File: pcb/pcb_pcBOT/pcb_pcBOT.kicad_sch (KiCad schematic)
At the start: 0 parts

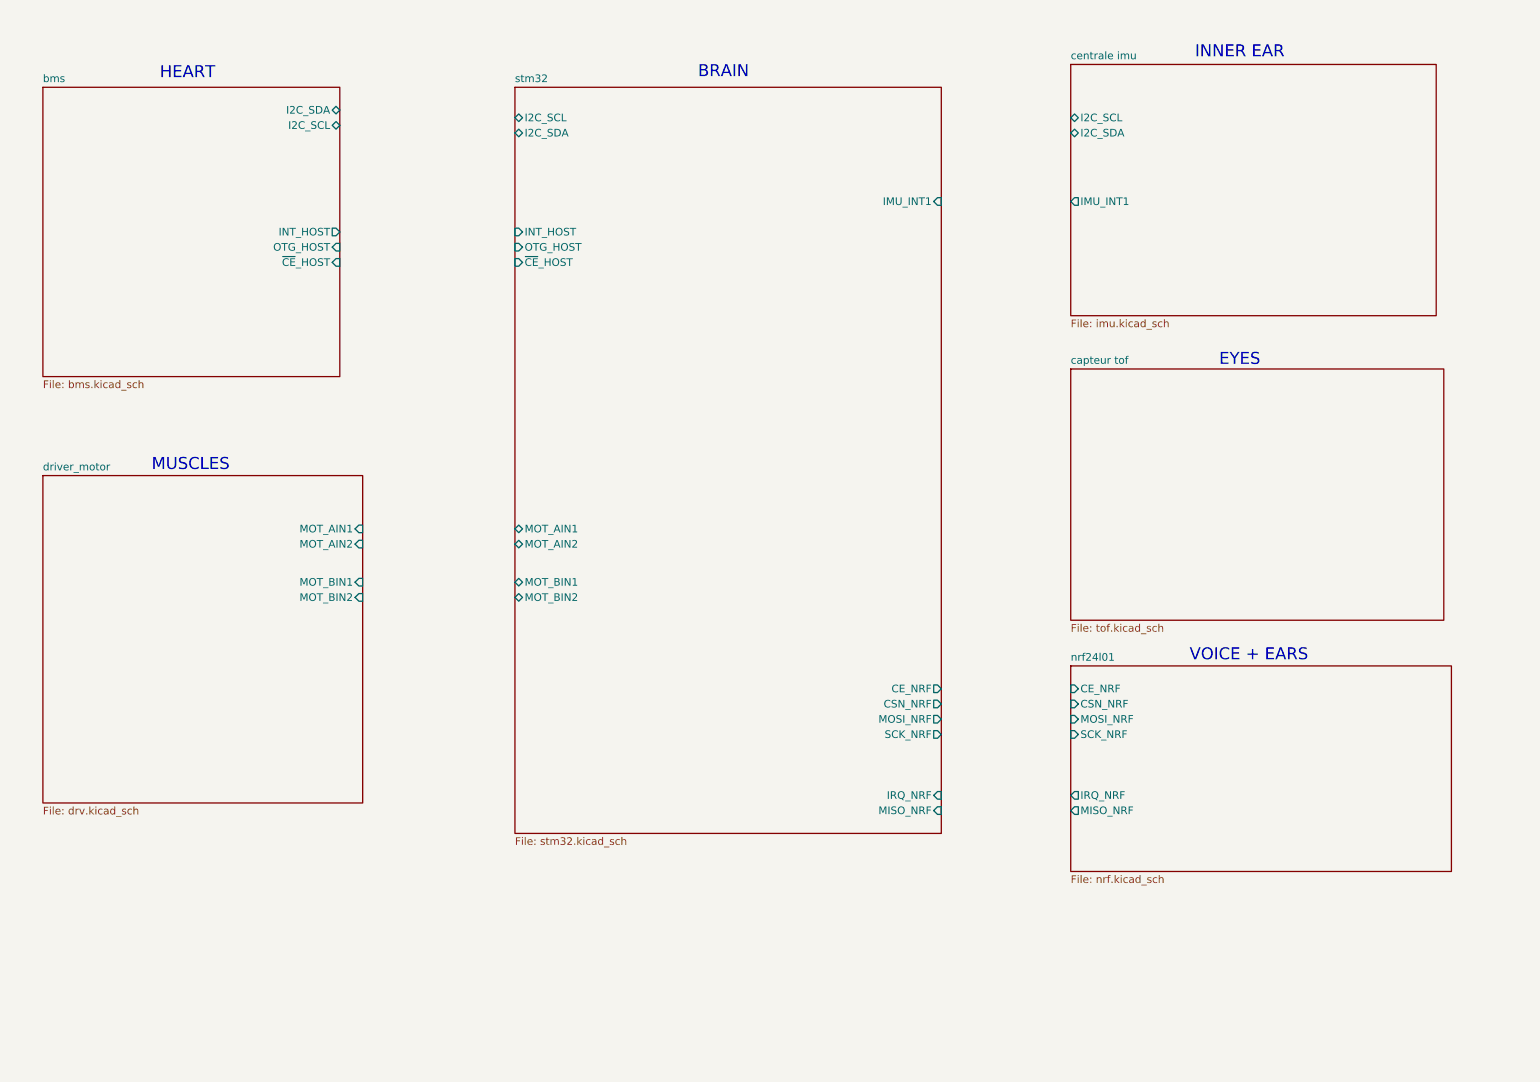
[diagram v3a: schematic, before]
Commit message: complement tof et connections, mise a jour du firmware
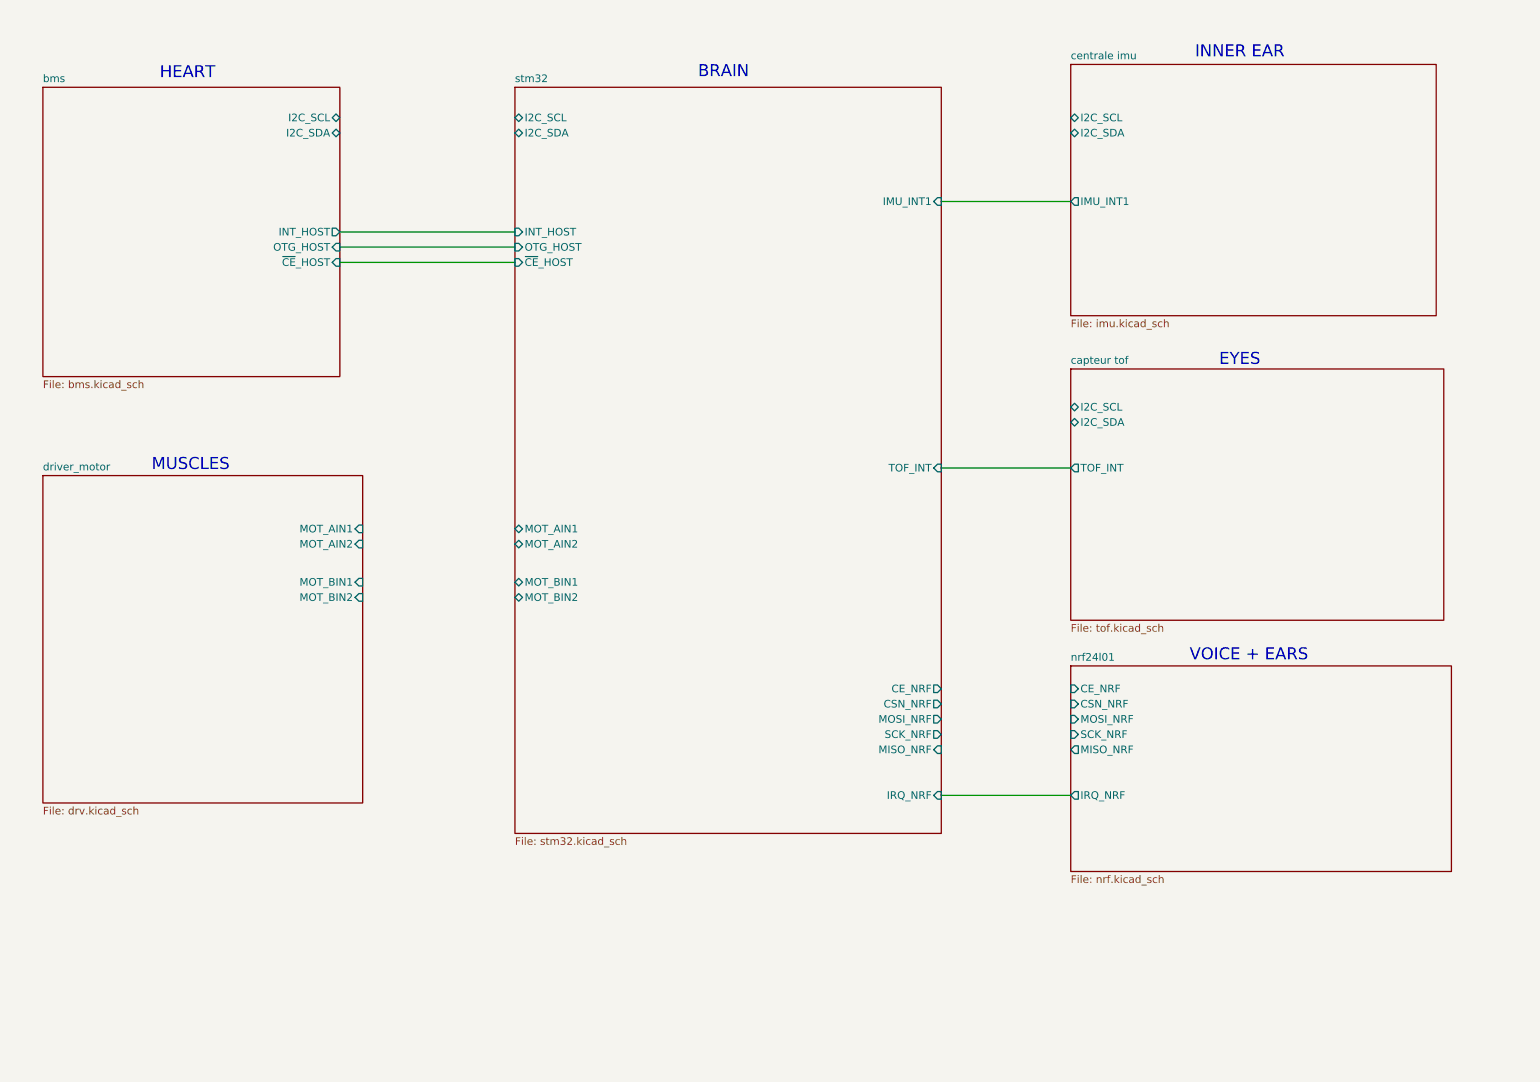
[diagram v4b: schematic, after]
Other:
- sheet capteur tof ports: added I2C_SCL, I2C_SDA, TOF_INT; removed none
- sheet stm32 ports: added TOF_INT; removed none
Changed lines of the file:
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@@
+		)
+	)
+	(wire
+		(pts
+			(xy 177.8 91.44) (xy 199.39 91.44)
+		)
+		(stroke
+			(width 0)
+			(type default)
+		)
+	)
+	(wire
+		(pts
+			(xy 177.8 46.99) (xy 199.39 46.99)
+		)
+		(stroke
+			(width 0)
+			(type default)
+		)
+	)
+	(wire
+		(pts
+			(xy 77.47 57.15) (xy 106.68 57.15)
+		)
+		(stroke
+			(width 0)
+			(type default)
+		)
+	)
+	(wire
+		(pts
+			(xy 177.8 146.05) (xy 199.39 146.05)
+		)
+		(stroke
+			(width 0)
+			(type default)
+		)
+	)
+	(wire
+		(pts
+			(xy 77.47 52.07) (xy 106.68 52.07)
+		)
+		(stroke
+			(width 0)
+			(type default)
+		)
+	)
+	(wire
+		(pts
+			(xy 77.47 54.61) (xy 106.68 54.61)
+		)
+		(stroke
+			(width 0)
+			(type default)
 		)
 	)
@@
 		)
 		(pin "MISO_NRF" output
-			(at 199.39 148.59 180)
+			(at 199.39 138.43 180)
 			(effects
 				(font
@@
 			)
 		)
+		(pin "TOF_INT" output
+			(at 199.39 91.44 180)
+			(effects
+				(font
+					(size 1.27 1.27)
+				)
+				(justify left)
+			)
+		)
+		(pin "I2C_SCL" bidirectional
+			(at 199.39 81.28 180)
+			(effects
+				(font
+					(size 1.27 1.27)
+				)
+				(justify left)
+			)
+		)
+		(pin "I2C_SDA" bidirectional
+			(at 199.39 83.82 180)
+			(effects
+				(font
+					(size 1.27 1.27)
+				)
+				(justify left)
+			)
+		)
 		(instances
 			(project "pcb_pcBOT"
@@
 		)
 		(pin "MISO_NRF" input
-			(at 177.8 148.59 0)
+			(at 177.8 138.43 0)
 			(effects
 				(font
@@
 		(pin "SCK_NRF" output
 			(at 177.8 135.89 0)
+			(effects
+				(font
+					(size 1.27 1.27)
+				)
+				(justify right)
+			)
+		)
+		(pin "TOF_INT" input
+			(at 177.8 91.44 0)
 			(effects
 				(font
@@
 		)
 		(pin "I2C_SDA" bidirectional
-			(at 77.47 31.75 0)
+			(at 77.47 35.56 0)
 			(effects
 				(font
@@
 		)
 		(pin "I2C_SCL" bidirectional
-			(at 77.47 34.29 0)
-			(effects
-				(font
+			(at 77.47 33.02 0)
+			(effects
+				(font

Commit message: corrections d'erreurs et liasons bus i2c et spi
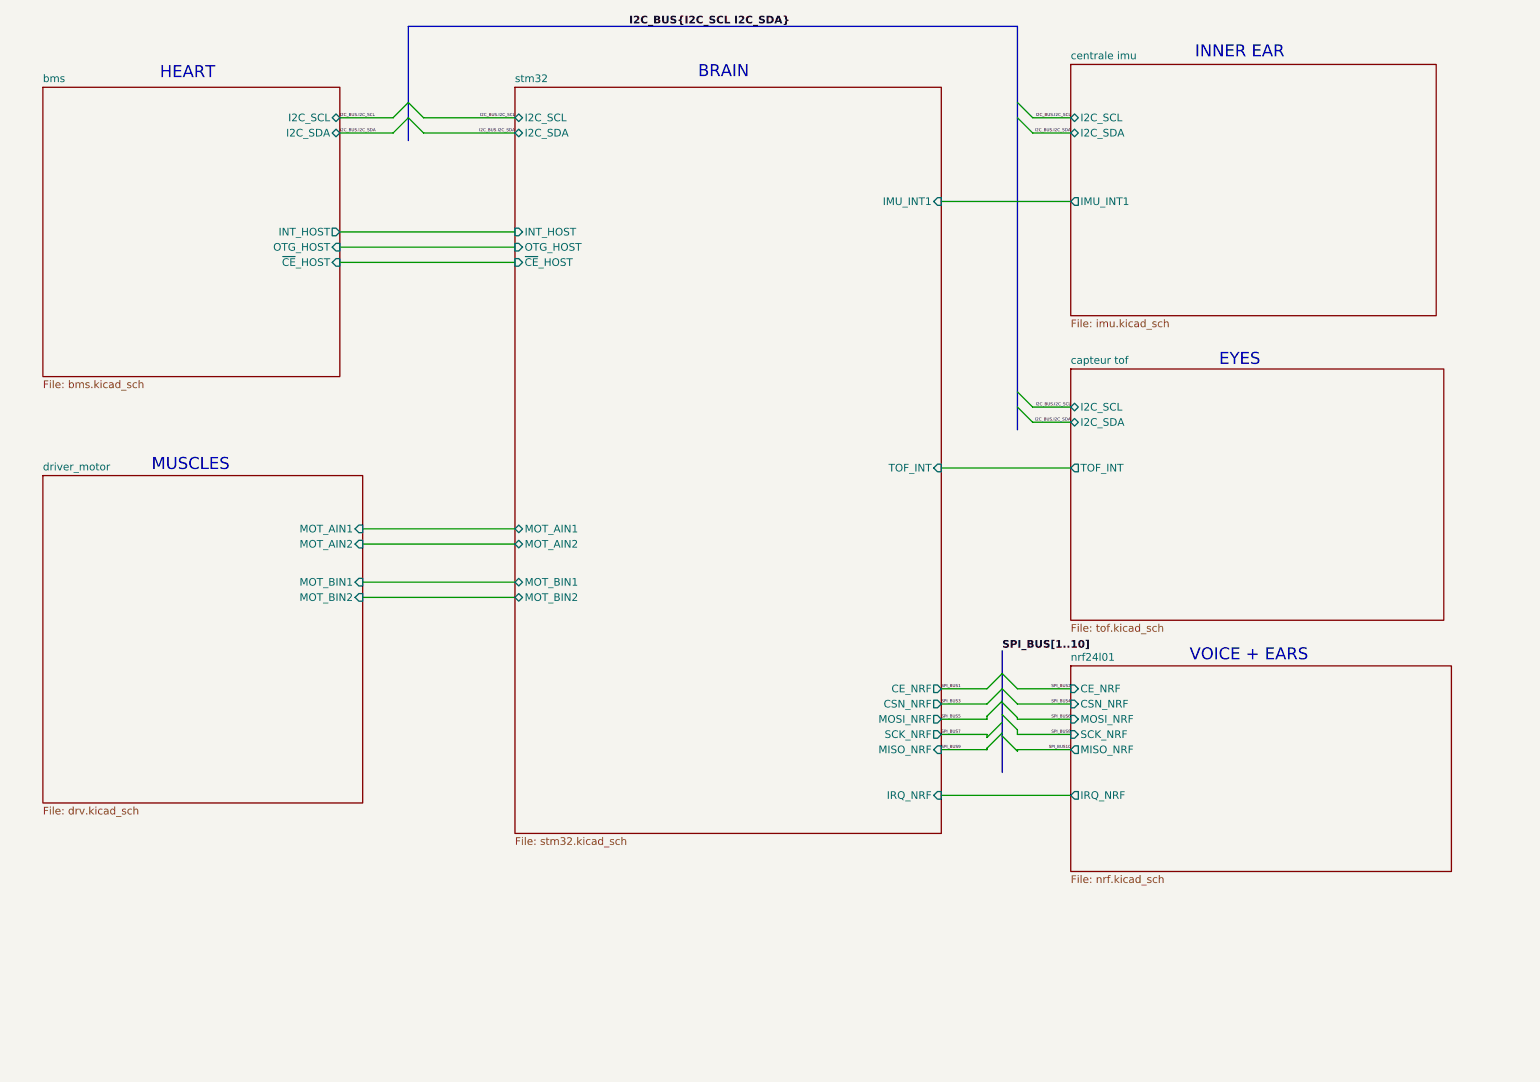
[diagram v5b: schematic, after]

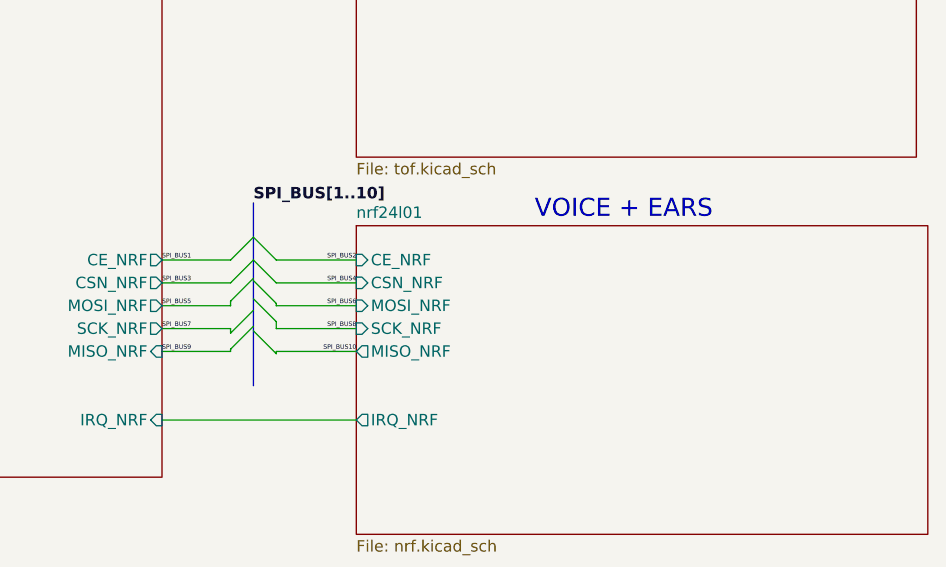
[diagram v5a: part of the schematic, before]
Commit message: Ajout empreintes (incomplet) + test erc correct
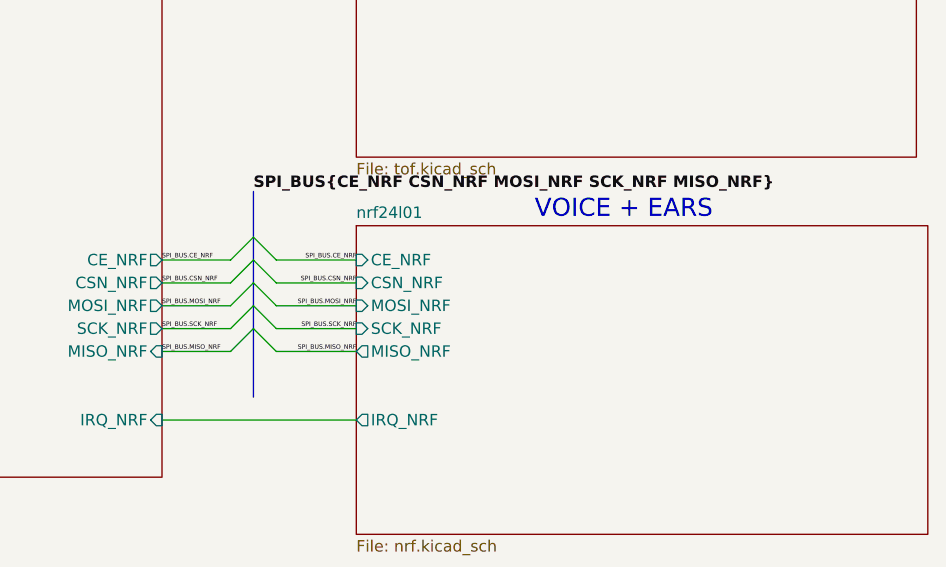
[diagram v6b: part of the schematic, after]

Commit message: fin de schematique
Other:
- sheet bms ports: added INT_BMS; removed INT_HOST
- sheet capteur tof ports: added TOF_INT1, TOF_INT2, TOF_INT3, XSHUT1, XSHUT2, XSHUT3; removed TOF_INT
- sheet stm32 ports: added INT_BMS, TOF_INT1, TOF_INT2, TOF_INT3, XSHUT1, XSHUT2, XSHUT3; removed INT_HOST, TOF_INT
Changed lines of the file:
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@@
-	(wire
-		(pts
-			(xy 177.8 91.44) (xy 199.39 91.44)
-		)
-		(stroke
-			(width 0)
-			(type default)
-		)
-	)
 	(wire
 		(pts
@@
 		)
 	)
+	(wire
+		(pts
+			(xy 177.8 104.14) (xy 199.39 104.14)
+		)
+		(stroke
+			(width 0)
+			(type default)
+		)
+	)
 	(bus
 		(pts
@@
 	(wire
 		(pts
+			(xy 177.8 99.06) (xy 199.39 99.06)
+		)
+		(stroke
+			(width 0)
+			(type default)
+		)
+	)
+	(wire
+		(pts
 			(xy 77.47 52.07) (xy 106.68 52.07)
 		)
@@
 		)
 	)
+	(wire
+		(pts
+			(xy 177.8 109.22) (xy 199.39 109.22)
+		)
+		(stroke
+			(width 0)
+			(type default)
+		)
+	)
 	(bus
 		(pts
@@
 	(wire
 		(pts
+			(xy 177.8 106.68) (xy 199.39 106.68)
+		)
+		(stroke
+			(width 0)
+			(type default)
+		)
+	)
+	(wire
+		(pts
 			(xy 81.28 101.6) (xy 106.68 101.6)
 		)
@@
 	(wire
 		(pts
+			(xy 177.8 101.6) (xy 199.39 101.6)
+		)
+		(stroke
+			(width 0)
+			(type default)
+		)
+	)
+	(wire
+		(pts
 			(xy 86.36 35.56) (xy 77.47 35.56)
 		)
@@
 		(pts
 			(xy 190.5 135.89) (xy 199.39 135.89)
+		)
+		(stroke
+			(width 0)
+			(type default)
+		)
+	)
+	(wire
+		(pts
+			(xy 177.8 96.52) (xy 199.39 96.52)
 		)
 		(stroke
@@
 		(effects
 			(font
-				(size 1.27 1.27)
+				(size 1 1)
 				(thickness 0.254)
 				(bold yes)
@@
 		)
 		(property "Sheetfile" "tof.kicad_sch"
-			(at 199.39 117.4246 0)
-			(effects
-				(font
-					(size 1.27 1.27)
+			(at 199.39 117.3166 0)
+			(effects
+				(font
+					(size 1 1)
 				)
 				(justify left top)
-			)
-		)
-		(pin "TOF_INT" output
-			(at 199.39 91.44 180)
-			(effects
-				(font
-					(size 1.27 1.27)
-				)
-				(justify left)
 			)
 		)
@@
 		(pin "I2C_SDA" bidirectional
 			(at 199.39 83.82 180)
+			(effects
+				(font
+					(size 1.27 1.27)
+				)
+				(justify left)
+			)
+		)
+		(pin "TOF_INT1" output
+			(at 199.39 96.52 180)
+			(effects
+				(font
+					(size 1.27 1.27)
+				)
+				(justify left)
+			)
+		)
+		(pin "TOF_INT2" output
+			(at 199.39 99.06 180)
+			(effects
+				(font
+					(size 1.27 1.27)
+				)
+				(justify left)
+			)
+		)
+		(pin "TOF_INT3" output
+			(at 199.39 101.6 180)
+			(effects
+				(font
+					(size 1.27 1.27)
+				)
+				(justify left)
+			)
+		)
+		(pin "XSHUT1" input
+			(at 199.39 104.14 180)
+			(effects
+				(font
+					(size 1.27 1.27)
+				)
+				(justify left)
+			)
+		)
+		(pin "XSHUT2" input
+			(at 199.39 106.68 180)
+			(effects
+				(font
+					(size 1.27 1.27)
+				)
+				(justify left)
+			)
+		)
+		(pin "XSHUT3" input
+			(at 199.39 109.22 180)
 			(effects
 				(font
@@
 			)
 		)
-		(pin "INT_HOST" input
+		(pin "INT_BMS" input
 			(at 106.68 52.07 180)
 			(effects
@@
 			)
 		)
-		(pin "TOF_INT" input
-			(at 177.8 91.44 0)
+		(pin "TOF_INT1" input
+			(at 177.8 96.52 0)
+			(effects
+				(font
+					(size 1.27 1.27)
+				)
+				(justify right)
+			)
+		)
+		(pin "TOF_INT2" input
+			(at 177.8 99.06 0)
+			(effects
+				(font
+					(size 1.27 1.27)
+				)
+				(justify right)
+			)
+		)
+		(pin "TOF_INT3" input
+			(at 177.8 101.6 0)
+			(effects
+				(font
+					(size 1.27 1.27)
+				)
+				(justify right)
+			)
+		)
+		(pin "XSHUT1" output
+			(at 177.8 104.14 0)
+			(effects
+				(font
+					(size 1.27 1.27)
+				)
+				(justify right)
+			)
+		)
+		(pin "XSHUT2" output
+			(at 177.8 106.68 0)
+			(effects
+				(font
+					(size 1.27 1.27)
+				)
+				(justify right)
+			)
+		)
+		(pin "XSHUT3" output
+			(at 177.8 109.22 0)
 			(effects
 				(font
@@
 			)
 		)
-		(pin "INT_HOST" output
+		(pin "INT_BMS" output
 			(at 77.47 52.07 0)
 			(effects

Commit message: rouatage + firmware wip
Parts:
- added H101, H102, H103, H104: MountingHole_Pad, MountingHole:MountingHole_3.2mm_M3_Pad_Via, symbol Mechanical:MountingHole_Pad
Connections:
- new net GND: H101.1, H102.1, H103.1, H104.1
